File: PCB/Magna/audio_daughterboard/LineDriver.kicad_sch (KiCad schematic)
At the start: 43 parts, among them J1301 PSG01550, U1301 NE5532, U1302 NE5532, U1303 NE5532

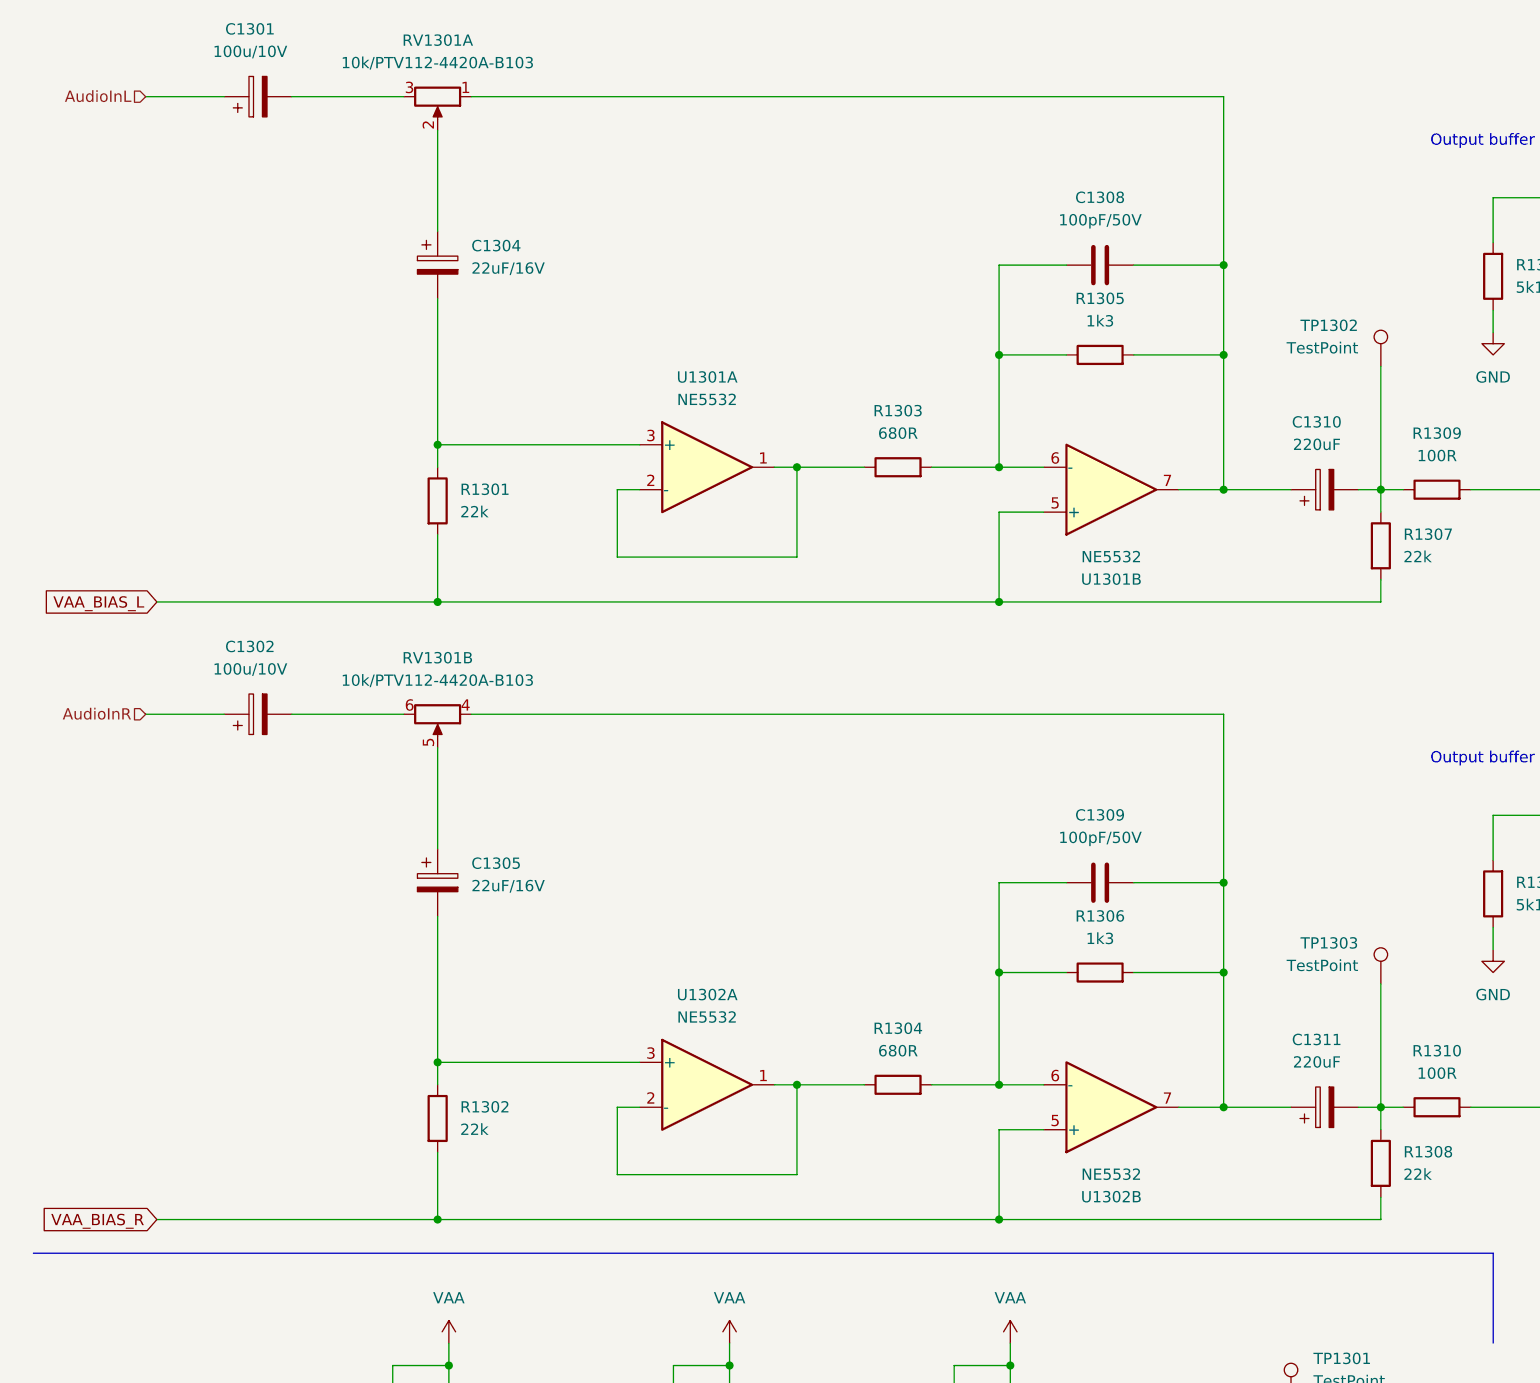
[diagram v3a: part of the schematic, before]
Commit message: Change ADC and add MCU for IO control
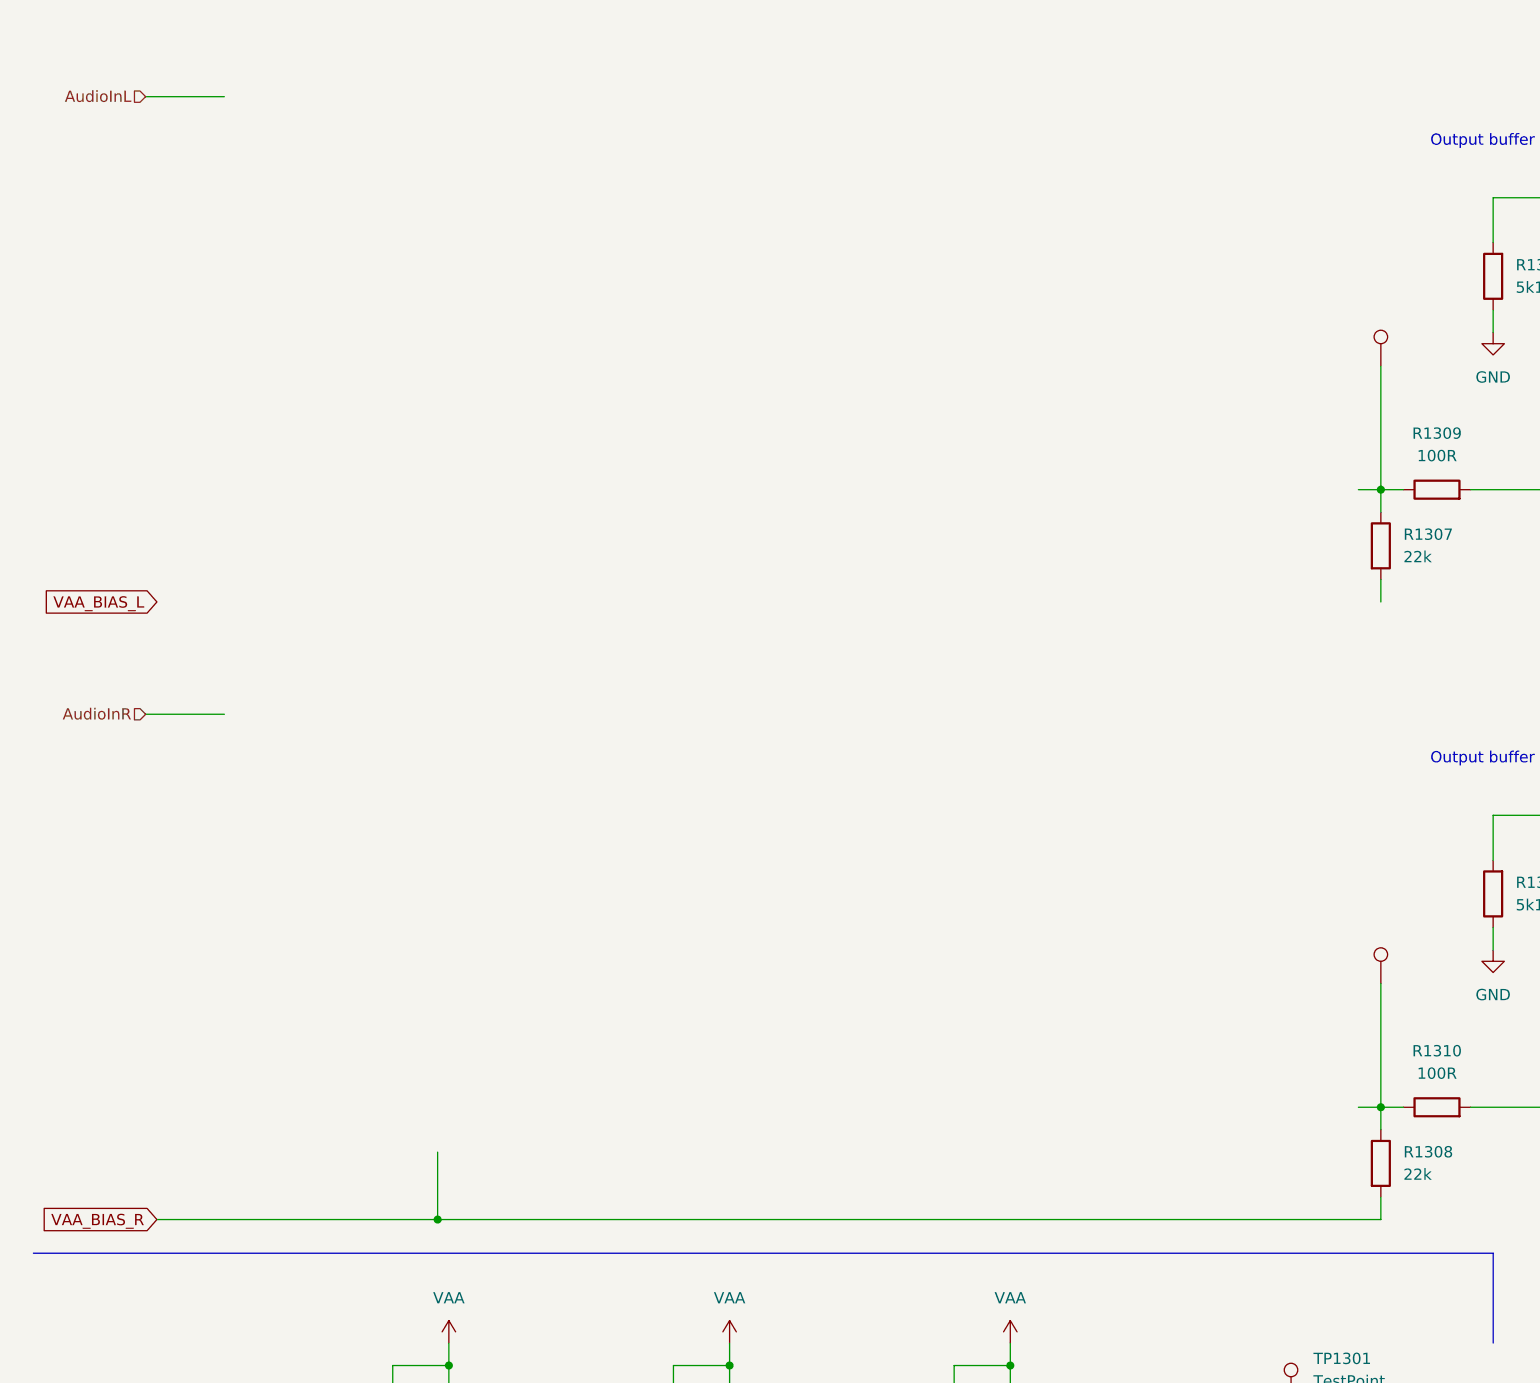
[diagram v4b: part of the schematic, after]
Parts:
- removed C1301, C1302: 100u/10V, Capacitor_SMD:CP_Elec_6.3x5.8, symbol Device:C_Polarized
- removed C1304, C1305: 22uF/16V, Capacitor_SMD:CP_Elec_5x5.8, symbol Device:C_Polarized
- removed C1308, C1309: 100pF/50V, Capacitor_SMD:C_0805_2012Metric_Pad1.18x1.45mm_HandSolder, symbol Device:C
- removed C1310, C1311: 220uF, Capacitor_SMD:CP_Elec_4x5.8, symbol Device:C_Polarized
- removed R1301, R1302: 22k, Resistor_SMD:R_0805_2012Metric_Pad1.20x1.40mm_HandSolder, symbol Device:R
- removed R1303, R1304: 680R, Resistor_SMD:R_0805_2012Metric_Pad1.20x1.40mm_HandSolder, symbol Device:R
- removed R1305, R1306: 1k3, Resistor_SMD:R_0805_2012Metric_Pad1.20x1.40mm_HandSolder, symbol Device:R
- removed RV1301: 10k/PTV112-4420A-B103, Skrooter_footprints:Potentiometer_Bourns_PTV09A-1_Dual_Vertical, symbol Device:R_Potentiometer_Dual_Separate
- removed unit 2 of U1301
- removed unit 1 of U1301
- removed unit 2 of U1302
- removed unit 1 of U1302
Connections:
- net VAA_BIAS_L: no longer R1307.2

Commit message: Some updates to PCB
Honestly I cannot remember whats changed
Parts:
- renumbered C1303 to C703, C1306 to C706, C1307 to C707, C1312 to C712, C1313 to C713, C1314 to C714, C1315 to C715, J1301 to J701, R1307 to R707, R1308 to R708, R1309 to R709, R1310 to R710, R1311 to R711, R1312 to R712, R1313 to R713, R1314 to R714, R1315 to R715, R1316 to R716, R1317 to R717, R1318 to R718, TP1301 to TP701, TP1302 to TP702, TP1303 to TP703, TP1304 to TP704, TP1305 to TP705, U1301 to U701, U1302 to U702, U1303 to U703

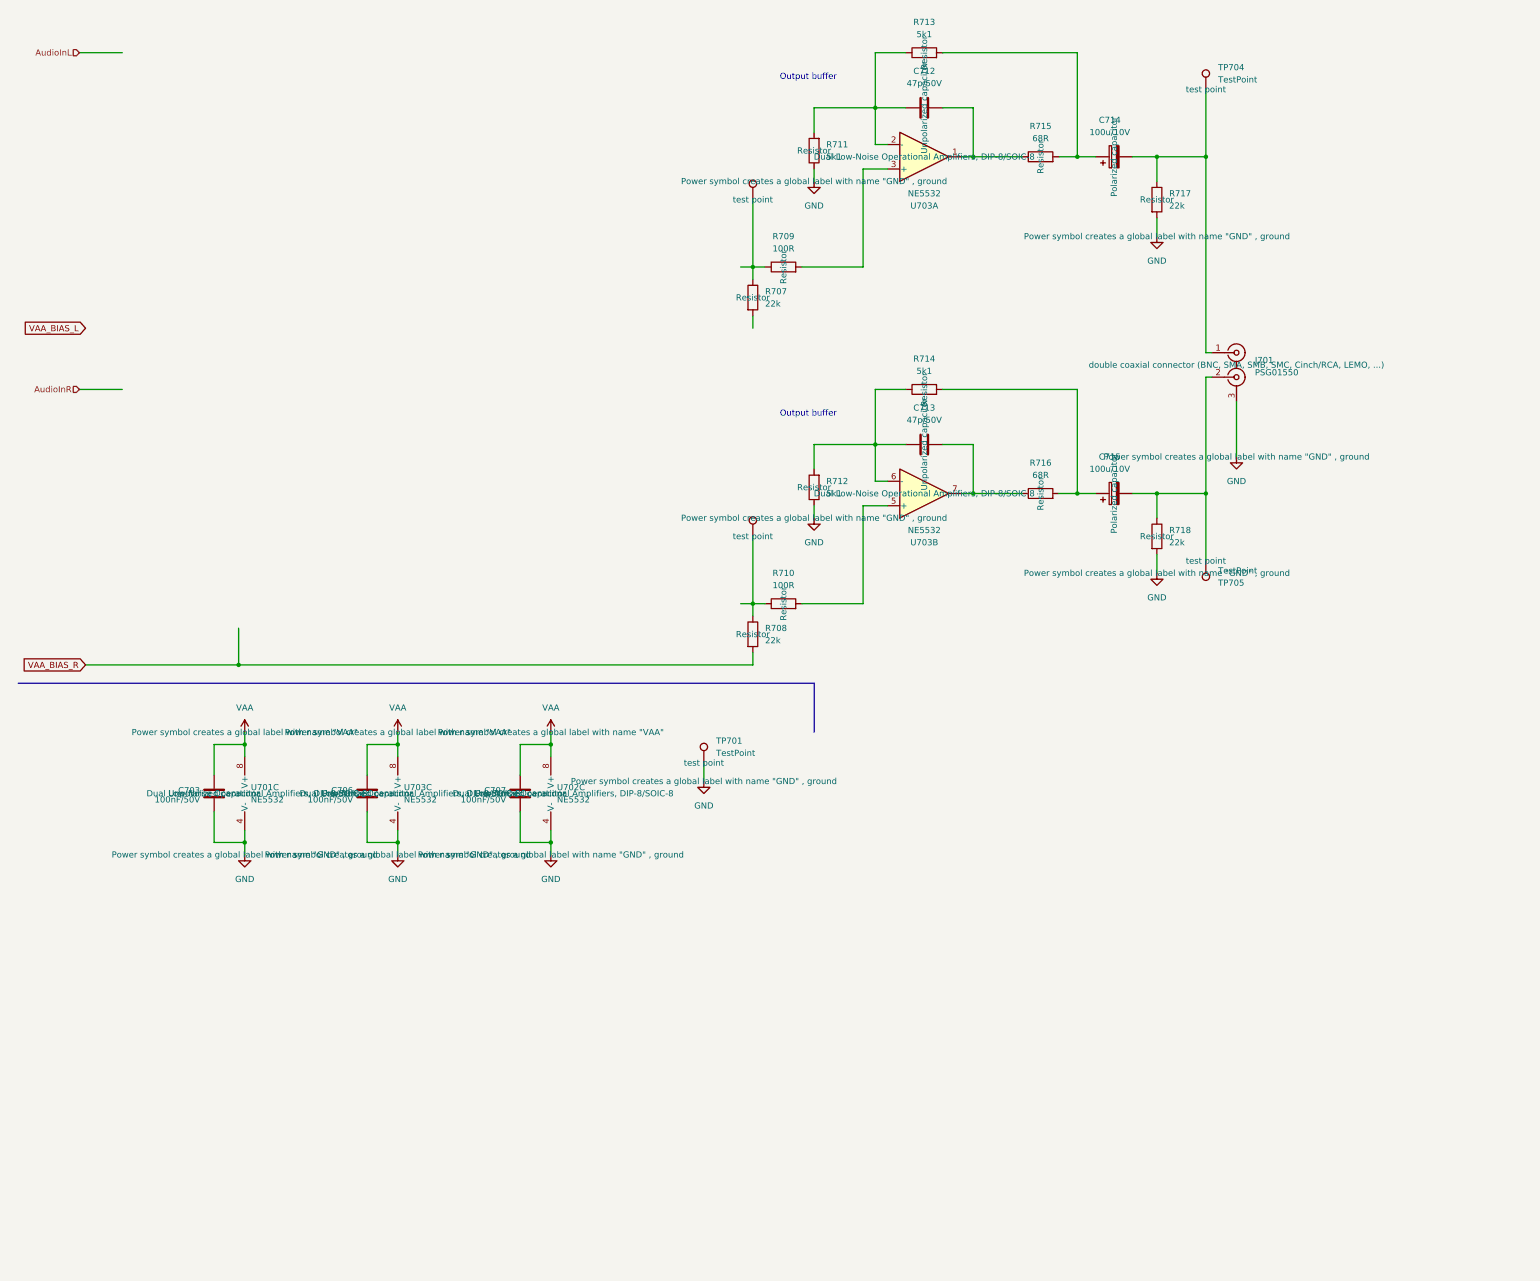
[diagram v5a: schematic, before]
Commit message: Update schematics to Kicad 9
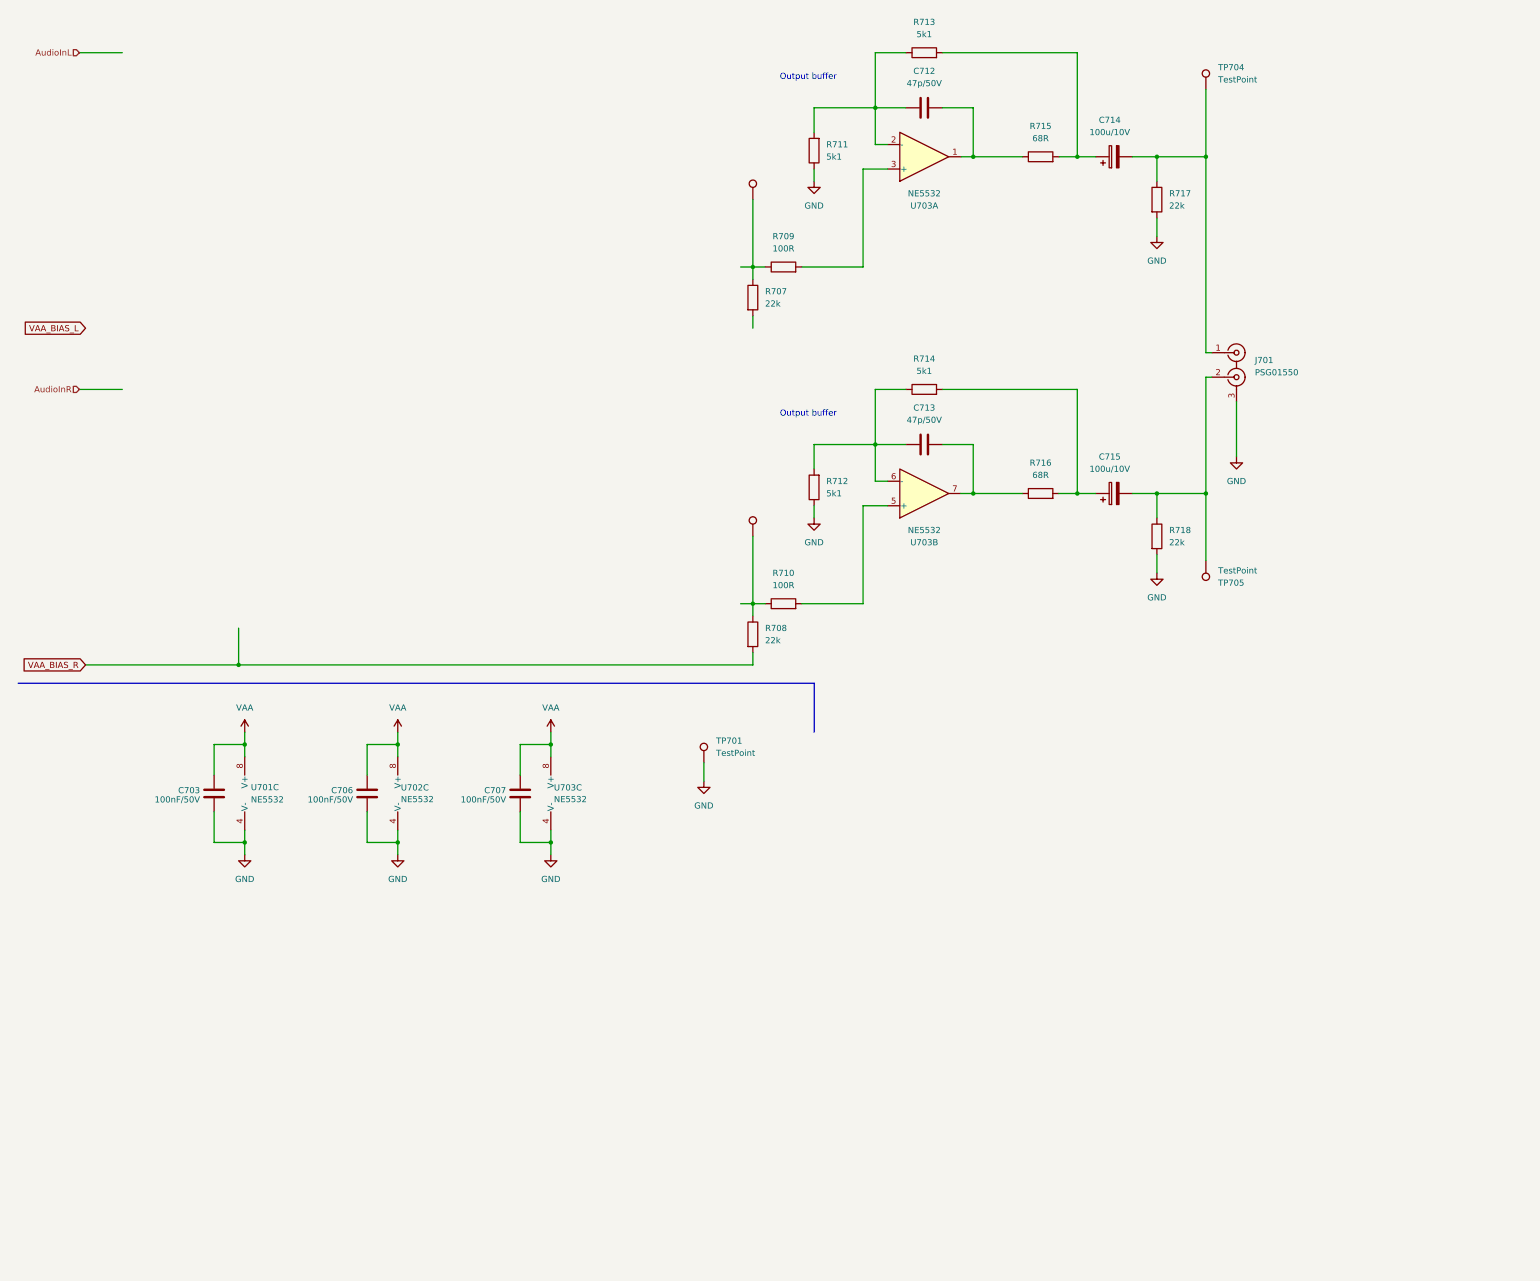
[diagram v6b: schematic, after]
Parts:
- renumbered U703 to U702, U702 to U703
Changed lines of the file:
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@@
 					(size 1.27 1.27)
 				)
+				(hide yes)
 			)
 		)
@@
 					(size 1.27 1.27)
 				)
+				(hide yes)
 			)
 		)
@@
 					(size 1.27 1.27)
 				)
+				(hide yes)
 			)
 		)
@@
 					(size 1.27 1.27)
 				)
+				(hide yes)
 			)
 		)
@@
 					(size 1.27 1.27)
 				)
+				(hide yes)
 			)
 		)
@@
 					(size 1.27 1.27)
 				)
+				(hide yes)
 			)
 		)
@@
 					(size 1.27 1.27)
 				)
+				(hide yes)
 			)
 		)
@@
 					(size 1.27 1.27)
 				)
+				(hide yes)
 			)
 		)
@@
 					(size 1.27 1.27)
 				)
+				(hide yes)
 			)
 		)
@@
 					(size 1.27 1.27)
 				)
+				(hide yes)
 			)
 		)
@@
 					(size 1.27 1.27)
 				)
+				(hide yes)
 			)
 		)
@@
 					(size 1.27 1.27)
 				)
+				(hide yes)
 			)
 		)
@@
 					(size 1.27 1.27)
 				)
+				(hide yes)
 			)
 		)
@@
 					(size 1.27 1.27)
 				)
+				(hide yes)
 			)
 		)
@@
 					(size 1.27 1.27)
 				)
+				(hide yes)
 			)
 		)
@@
 					(size 1.27 1.27)
 				)
+				(hide yes)
 			)
 		)
@@
 					(size 1.27 1.27)
 				)
+				(hide yes)
 			)
 		)
@@
 					(size 1.27 1.27)
 				)
+				(hide yes)
 			)
 		)
@@
 					(size 1.27 1.27)
 				)
+				(hide yes)
 			)
 		)
@@
 					(size 1.27 1.27)
 				)
+				(hide yes)
 			)
 		)
@@
 					(size 1.27 1.27)
 				)
+				(hide yes)
 			)
 		)
@@
 					(size 1.27 1.27)
 				)
+				(hide yes)
 			)
 		)
@@
 					(size 1.27 1.27)
 				)
+				(hide yes)
 			)
 		)
@@
 					(size 1.27 1.27)
 				)
+				(hide yes)
 			)
 		)
@@
 					(size 1.27 1.27)
 				)
+				(hide yes)
 			)
 		)
@@
 					(size 1.27 1.27)
 				)
+				(hide yes)
 			)
 		)
@@
 					(size 1.27 1.27)
 				)
+				(hide yes)
 			)
 		)
@@
 					(size 1.27 1.27)
 				)
+				(hide yes)
 			)
 		)
@@
 					(size 1.27 1.27)
 				)
+				(hide yes)
 			)
 		)
@@
 		(dnp no)
 		(fields_autoplaced yes)
-		(property "Reference" "U702"
-			(at 124.46 176.53 0)
+		(property "Reference" "U703"
+			(at 123.825 176.5878 0)
 			(effects
 				(font
@@
 		)
 		(property "Value" "NE5532"
-			(at 124.46 179.07 0)
+			(at 123.825 179.0121 0)
 			(effects
 				(font
@@
 					(size 1.27 1.27)
 				)
+				(hide yes)
 			)
 		)
@@
 			(project "Audio_daughterboard"
 				(path "/1eadd930-2484-4c28-b568-78e6454e7f52/9bed4810-f3e5-480b-be82-dd0796c0885f"
-					(reference "U702")
+					(reference "U703")
 					(unit 3)
 				)
@@
 					(size 1.27 1.27)
 				)
+				(hide yes)
 			)
 		)
@@
 		(dnp no)
 		(fields_autoplaced yes)
-		(property "Reference" "U703"
-			(at 92.71 176.53 0)
+		(property "Reference" "U702"
+			(at 92.075 176.5878 0)
 			(effects
 				(font
@@
 		)
 		(property "Value" "NE5532"
-			(at 92.71 179.07 0)
+			(at 92.075 179.0121 0)
 			(effects
 				(font
@@
 					(size 1.27 1.27)
 				)
+				(hide yes)
 			)
 		)
@@
 			(project "Audio_daughterboard"
 				(path "/1eadd930-2484-4c28-b568-78e6454e7f52/9bed4810-f3e5-480b-be82-dd0796c0885f"
-					(reference "U703")
+					(reference "U702")
 					(unit 3)
 				)
@@
 					(size 1.27 1.27)
 				)
+				(hide yes)
 			)
 		)
@@
 					(size 1.27 1.27)
 				)
+				(hide yes)
 			)
 		)
@@
 					(size 1.27 1.27)
 				)
+				(hide yes)
 			)
 		)
@@
 					(size 1.27 1.27)
 				)
+				(hide yes)
 			)
 		)
@@
 					(size 1.27 1.27)
 				)
+				(hide yes)
 			)
 		)
@@
 					(size 1.27 1.27)
 				)
+				(hide yes)
 			)
 		)
@@
 					(size 1.27 1.27)
 				)
+				(hide yes)
 			)
 		)
@@
 					(size 1.27 1.27)
 				)
+				(hide yes)
 			)
 		)
@@
 					(size 1.27 1.27)
 				)
+				(hide yes)
 			)
 		)
@@
 					(size 1.27 1.27)
 				)
+				(hide yes)
 			)
 		)
